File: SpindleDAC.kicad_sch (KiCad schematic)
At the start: 9 parts, among them J13 0-10V Spindle Out, U24 LTV-817S, U25 ${SIM.PARAMS}

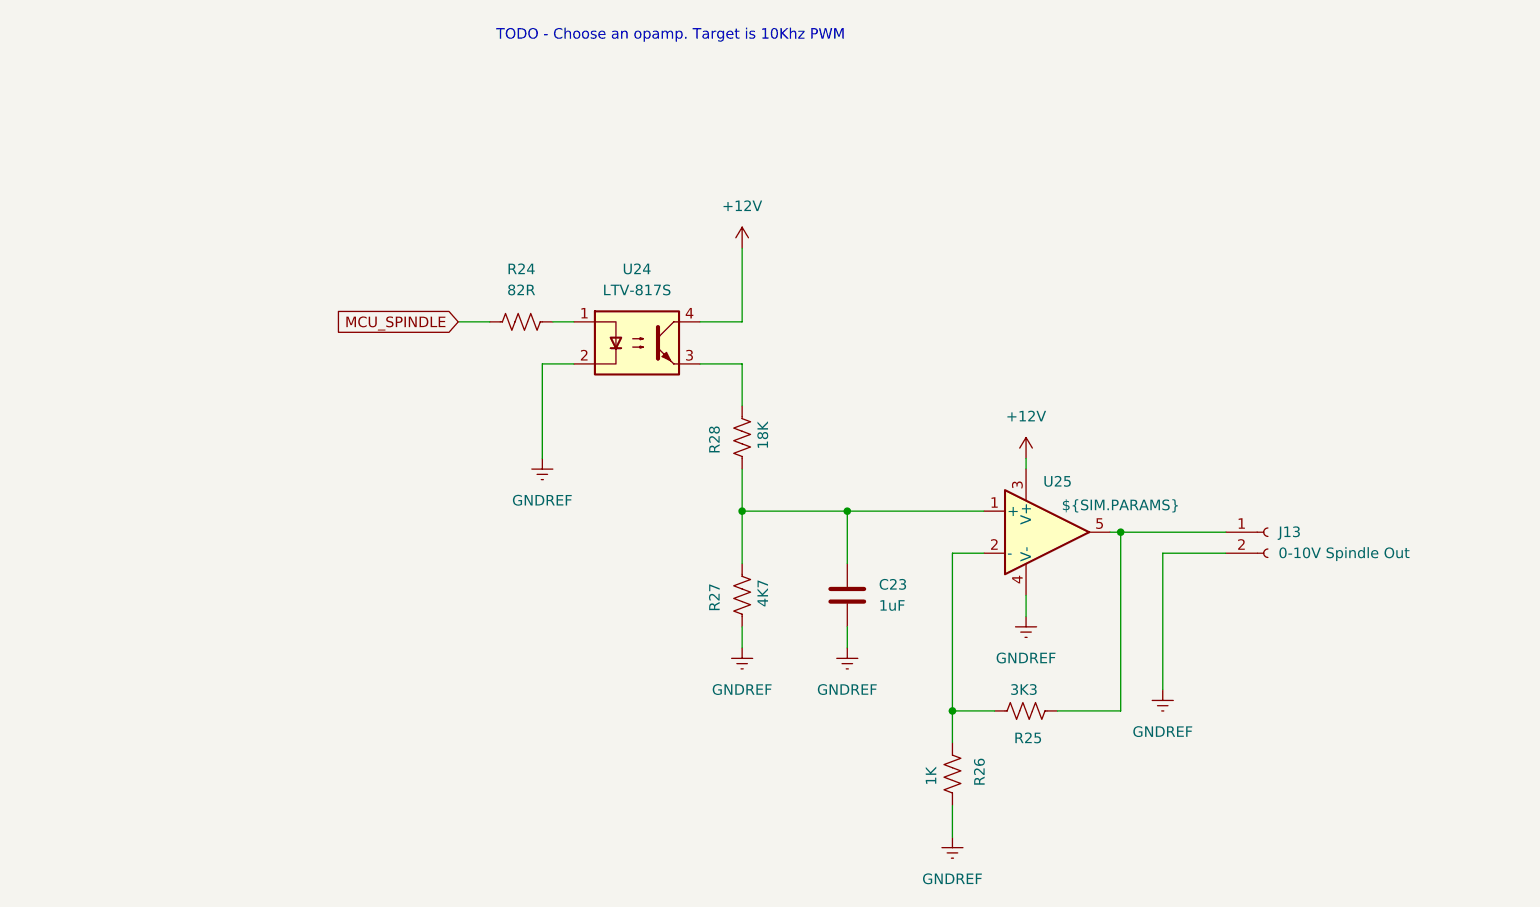
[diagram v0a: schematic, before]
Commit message: Simplified spindle DAC. Performs better in simulator.
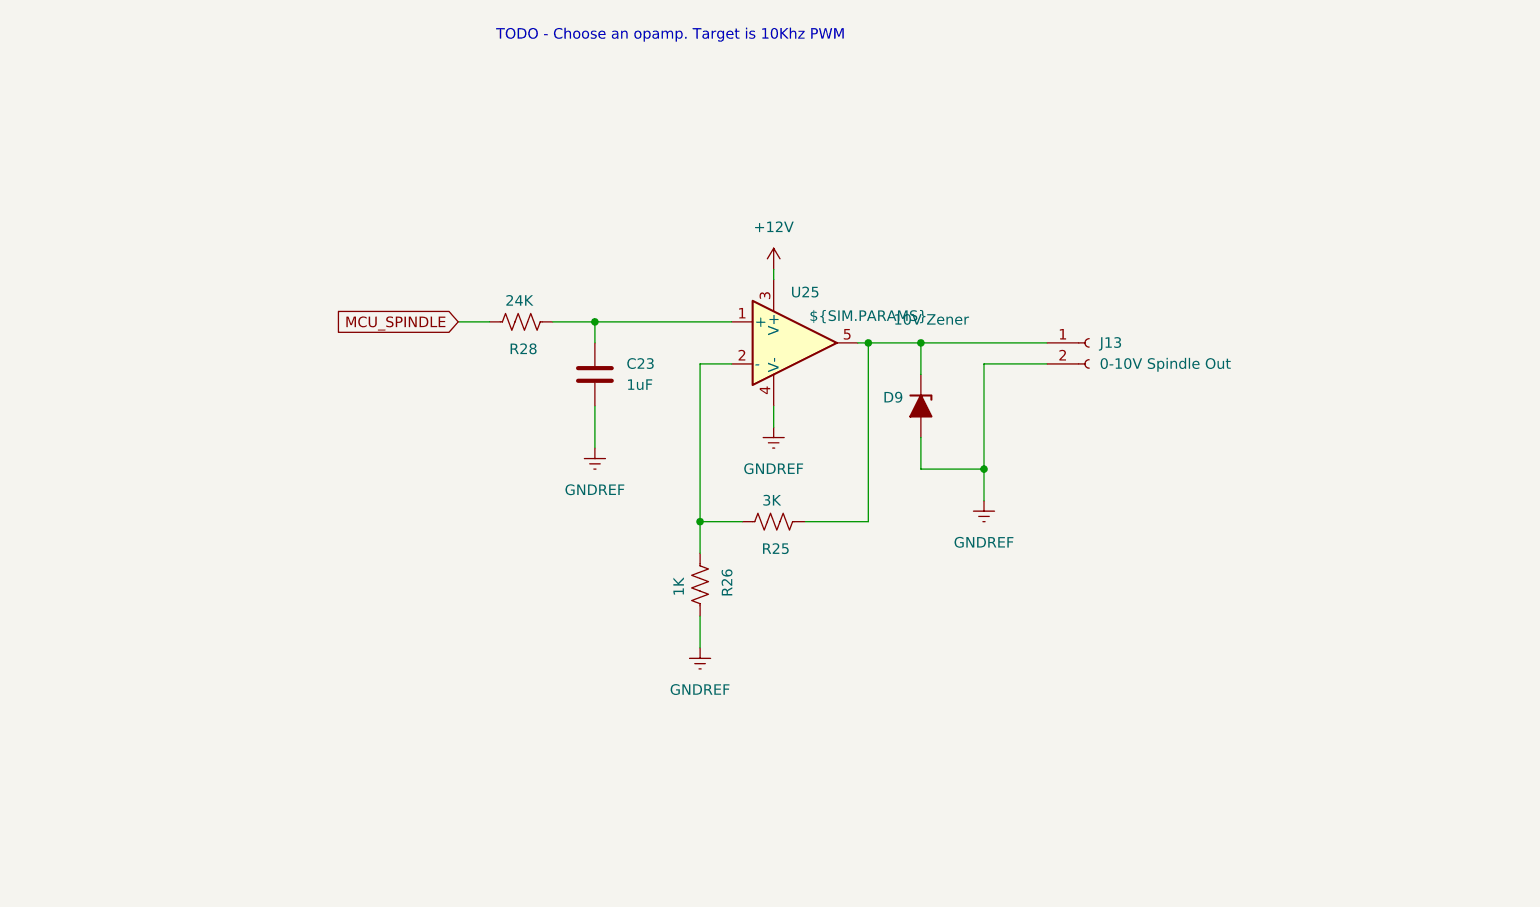
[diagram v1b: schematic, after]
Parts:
- removed R24: 82R, symbol Device:R_US
- removed R27: 4K7, symbol Device:R_US
- removed U24: LTV-817S, Package_SO:SOIC-16_3.9x9.9mm_P1.27mm, symbol Isolator:LTV-817S
- added D9: 10V Zener, symbol Device:D_Zener_Filled
- R25: value 3K3 -> 3K
- R28: value 18K -> 24K
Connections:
- net GNDREF: now also D9.2 (A)
- net MCU_SPINDLE: now also R28.2
- net at J13.1 (Pin_1), R25.1, U25.5: now also D9.1 (K)
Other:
- moved on the sheet: C23, J13, R25, R26, R28, U25

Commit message: buffered output on spindle DAC, tweak to gain structure and update to readme
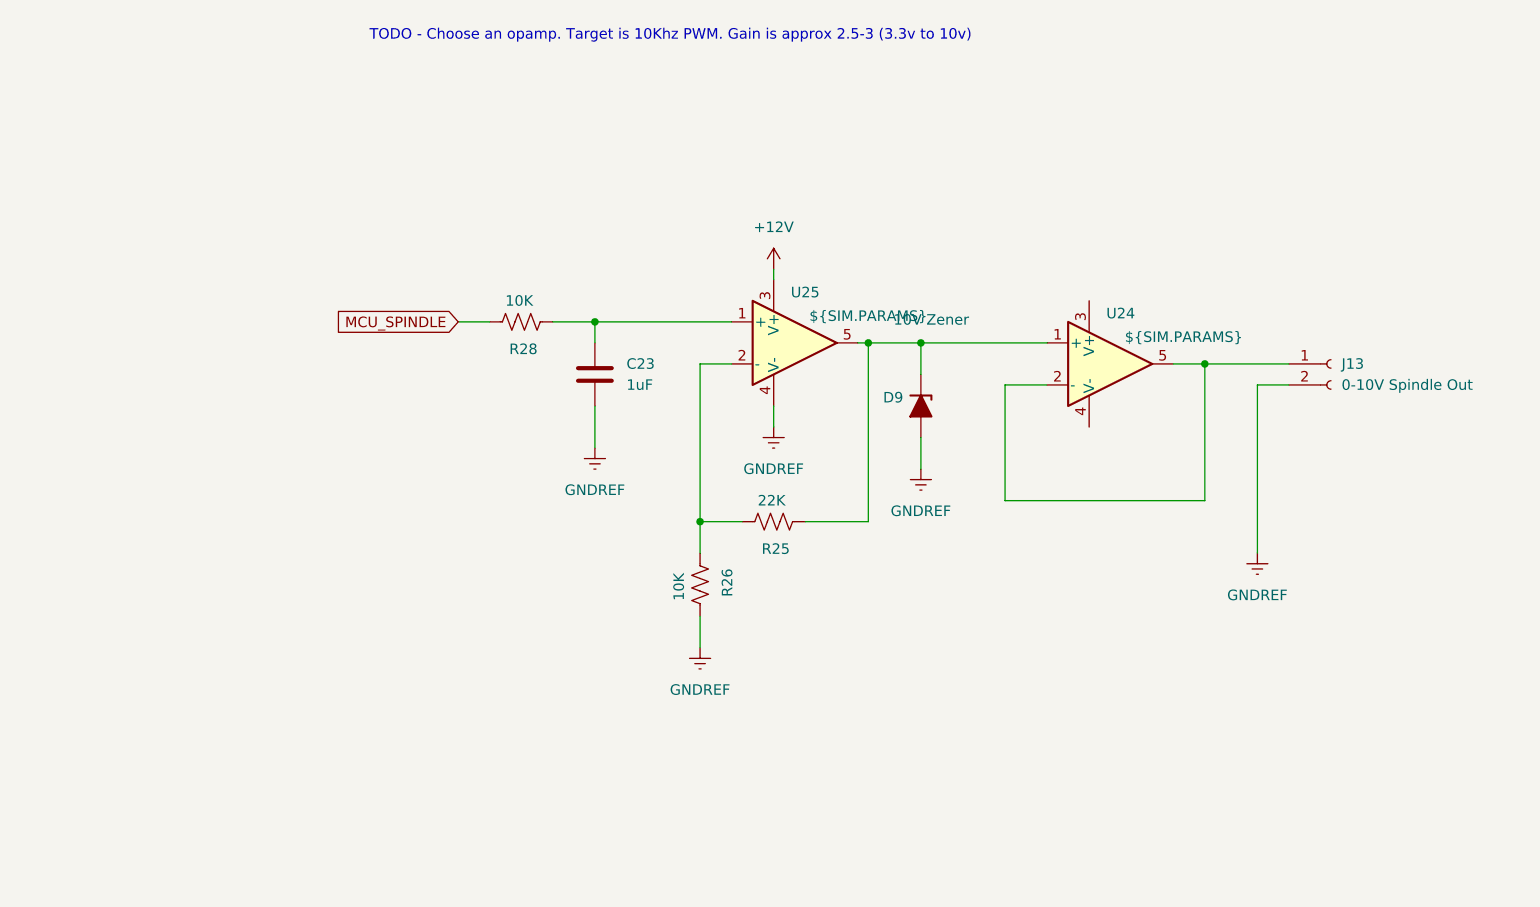
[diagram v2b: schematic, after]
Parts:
- added U24: ${SIM.PARAMS}, symbol Simulation_SPICE:OPAMP
- R25: value 3K -> 22K
- R26: value 1K -> 10K
- R28: value 24K -> 10K
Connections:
- net at D9.1 (K), R25.1, U25.5: now also U24.1 (+); no longer J13.1 (Pin_1)
- new net: J13.1 (Pin_1), U24.2 (-), U24.5
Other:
- note added: "TODO - Choose an opamp. Target is 10Khz PWM. Gain is approx 2.5-3 (3.3v to 10v)"
- note removed: "TODO - Choose an opamp. Target is 10Khz PWM"
- moved on the sheet: J13

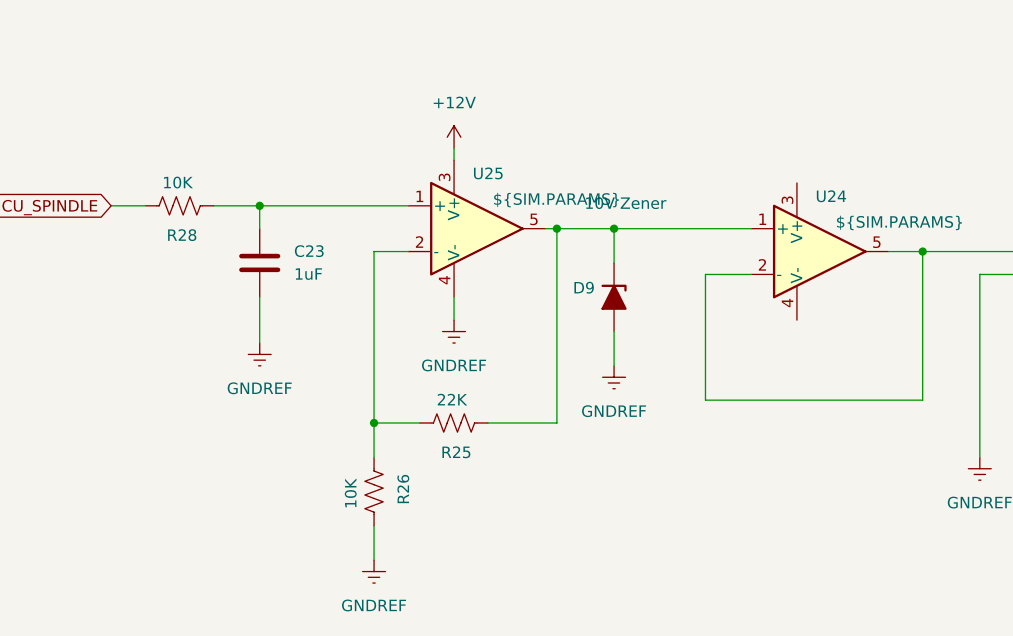
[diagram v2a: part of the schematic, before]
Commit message: Deleted stale test production files. Fixed up a bug with power isolation. Created some footprints for wire to board connectors although ran out of time to fix a bug where they do no lock in. Fixes to readme
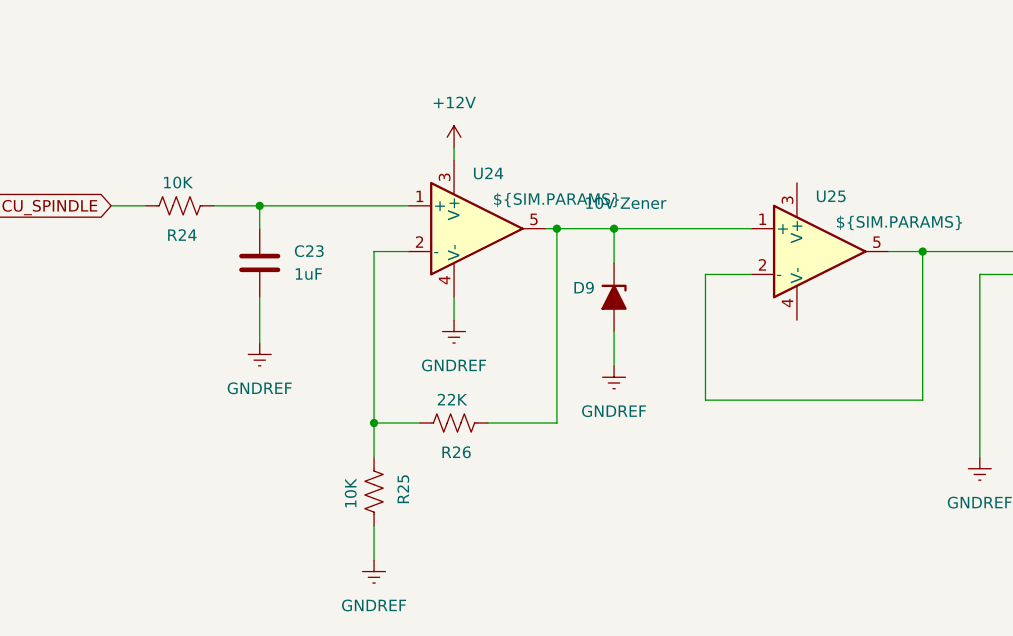
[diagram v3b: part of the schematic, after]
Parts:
- J13: footprint (none) -> OSTVTerminalBlocks:Conn01x02
- renumbered R28 to R24, R26 to R25, R25 to R26, U25 to U24, U24 to U25
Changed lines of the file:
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@@
 		(on_board yes)
 		(dnp no)
-		(property "Reference" "R26"
+		(property "Reference" "R25"
 			(at 126.492 102.616 90)
 			(effects
@@
 			(project "Remora Nucleo F446ZE Hat"
 				(path "/5473abc6-7b93-43cc-a401-f691c4d7d7cf/5cdad347-c6ad-4791-9d53-e4d1ad999196"
-					(reference "R26")
+					(reference "R25")
 					(unit 1)
 				)
@@
 		(dnp no)
 		(fields_autoplaced yes)
-		(property "Reference" "#PWR0144"
+		(property "Reference" "#PWR0141"
 			(at 132.08 90.17 0)
 			(effects
@@
 			(project "Remora Nucleo F446ZE Hat"
 				(path "/5473abc6-7b93-43cc-a401-f691c4d7d7cf/5cdad347-c6ad-4791-9d53-e4d1ad999196"
-					(reference "#PWR0144")
+					(reference "#PWR0141")
 					(unit 1)
 				)
@@
 		(on_board yes)
 		(dnp no)
-		(property "Reference" "U24"
+		(property "Reference" "U25"
 			(at 173.99 70.104 0)
 			(effects
@@
 			(project "Remora Nucleo F446ZE Hat"
 				(path "/5473abc6-7b93-43cc-a401-f691c4d7d7cf/5cdad347-c6ad-4791-9d53-e4d1ad999196"
-					(reference "U24")
+					(reference "U25")
 					(unit 1)
 				)
@@
 		(dnp no)
 		(fields_autoplaced yes)
-		(property "Reference" "#PWR0145"
+		(property "Reference" "#PWR0142"
 			(at 149.86 95.25 0)
 			(effects
@@
 			(project "Remora Nucleo F446ZE Hat"
 				(path "/5473abc6-7b93-43cc-a401-f691c4d7d7cf/5cdad347-c6ad-4791-9d53-e4d1ad999196"
-					(reference "#PWR0145")
+					(reference "#PWR0142")
 					(unit 1)
 				)
@@
 		(on_board yes)
 		(dnp no)
-		(property "Reference" "R25"
+		(property "Reference" "R26"
 			(at 132.334 98.552 90)
 			(effects
@@
 			(project "Remora Nucleo F446ZE Hat"
 				(path "/5473abc6-7b93-43cc-a401-f691c4d7d7cf/5cdad347-c6ad-4791-9d53-e4d1ad999196"
-					(reference "R25")
+					(reference "R26")
 					(unit 1)
 				)
@@
 		(on_board yes)
 		(dnp no)
-		(property "Reference" "#PWR0142"
+		(property "Reference" "#PWR0138"
 			(at 110.49 92.71 0)
 			(effects
@@
 			(project "Remora Nucleo F446ZE Hat"
 				(path "/5473abc6-7b93-43cc-a401-f691c4d7d7cf/5cdad347-c6ad-4791-9d53-e4d1ad999196"
-					(reference "#PWR0142")
+					(reference "#PWR0138")
 					(unit 1)
 				)
@@
 			)
 		)
-		(property "Footprint" ""
+		(property "Footprint" "OSTVTerminalBlocks:Conn01x02"
 			(at 199.39 76.2 0)
 			(effects
@@
 		(dnp no)
 		(fields_autoplaced yes)
-		(property "Reference" "#PWR0138"
+		(property "Reference" "#PWR0143"
 			(at 190.5 105.41 0)
 			(effects
@@
 			(project "Remora Nucleo F446ZE Hat"
 				(path "/5473abc6-7b93-43cc-a401-f691c4d7d7cf/5cdad347-c6ad-4791-9d53-e4d1ad999196"
-					(reference "#PWR0138")
+					(reference "#PWR0143")
 					(unit 1)
 				)
@@
 		(on_board yes)
 		(dnp no)
-		(property "Reference" "R28"
+		(property "Reference" "R24"
 			(at 101.854 74.422 90)
 			(effects
@@
 			(project "Remora Nucleo F446ZE Hat"
 				(path "/5473abc6-7b93-43cc-a401-f691c4d7d7cf/5cdad347-c6ad-4791-9d53-e4d1ad999196"
-					(reference "R28")
+					(reference "R24")
 					(unit 1)
 				)
@@
 		(on_board yes)
 		(dnp no)
-		(property "Reference" "U25"
+		(property "Reference" "U24"
 			(at 135.89 67.564 0)
 			(effects
@@
 			(project ""
 				(path "/5473abc6-7b93-43cc-a401-f691c4d7d7cf/5cdad347-c6ad-4791-9d53-e4d1ad999196"
-					(reference "U25")
+					(reference "U24")
 					(unit 1)
 				)
@@
 		(dnp no)
 		(fields_autoplaced yes)
-		(property "Reference" "#PWR0143"
+		(property "Reference" "#PWR0140"
 			(at 132.08 68.58 0)
 			(effects
@@
 			(project "Remora Nucleo F446ZE Hat"
 				(path "/5473abc6-7b93-43cc-a401-f691c4d7d7cf/5cdad347-c6ad-4791-9d53-e4d1ad999196"
-					(reference "#PWR0143")
-					(unit 1)
-				)
+					(reference "#PWR0140")
+					(unit 1)
+				)
